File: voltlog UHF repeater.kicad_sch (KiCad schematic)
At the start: 40 parts, among them J1 Conn_02x13_Odd_Even, J2 Conn_01x13, J3 Conn_Coaxial, Q1 BC847, Q2 BC857, U1 SA818

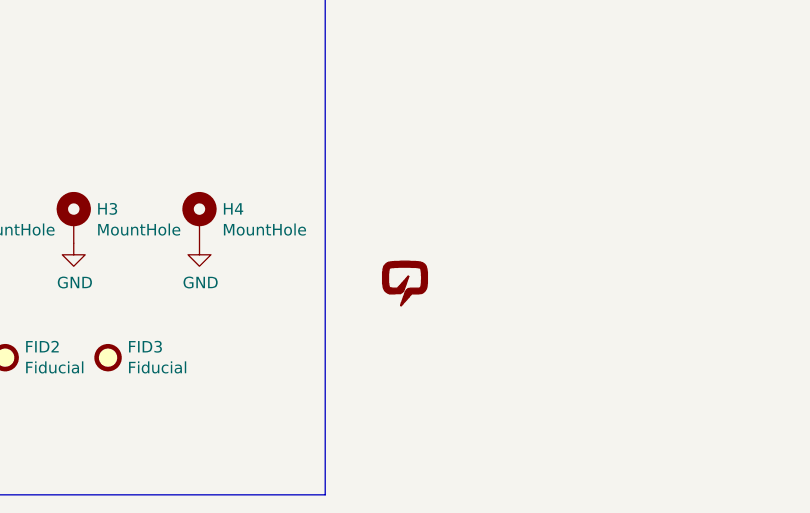
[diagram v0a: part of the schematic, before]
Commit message: Removed logo from schemantic. Removed H1-H4, Fid1-Fid3, J1, J2 and JP1 from BOM and POS file.
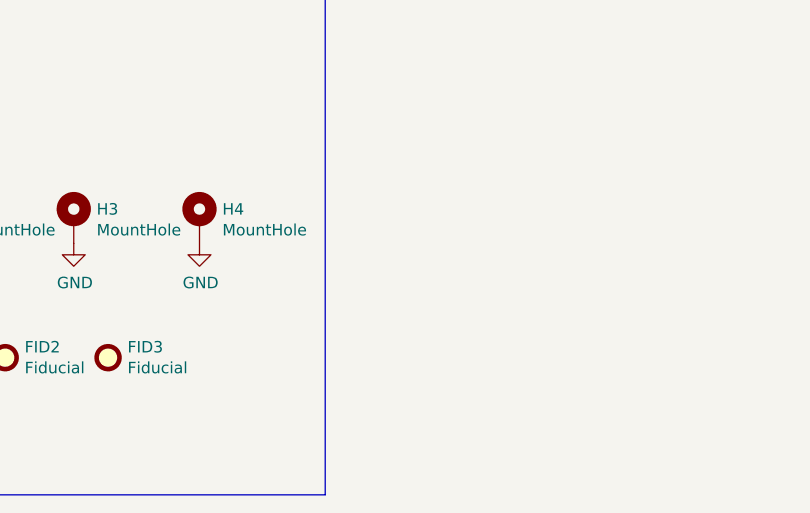
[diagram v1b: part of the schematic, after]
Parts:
- removed V1: VOLTLOG_LOGO, Voltlog:voltlog_mask_3mm, symbol voltlog UHF repeater-rescue:VOLTLOG_LOGO-voltlog
- H1, H2, H3, H4: now left out of the parts list
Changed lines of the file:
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@@
   )
   (symbol (lib_id "Connector_Generic:Conn_02x13_Odd_Even") (at 44.45 168.91 0) (unit 1)
-    (in_bom yes) (on_board yes) (dnp no)
+    (in_bom yes) (on_board no) (dnp no)
     (property "Reference" "J1" (at 45.72 148.1582 0)
       (effects (font (size 1.27 1.27)))
@@
   )
   (symbol (lib_id "Connector_Generic:Conn_01x13") (at 90.17 168.91 0) (unit 1)
-    (in_bom yes) (on_board yes) (dnp no)
+    (in_bom yes) (on_board no) (dnp no)
     (property "Reference" "J2" (at 92.202 167.8432 0)
       (effects (font (size 1.27 1.27)) (justify left))
@@
   )
   (symbol (lib_id "Mechanical:Fiducial") (at 127 179.07 0) (unit 1)
-    (in_bom no) (on_board yes) (dnp no)
+    (in_bom no) (on_board no) (dnp no)
     (property "Reference" "FID1" (at 129.159 177.9016 0)
       (effects (font (size 1.27 1.27)) (justify left))
@@
   )
   (symbol (lib_id "Mechanical:Fiducial") (at 138.43 179.07 0) (unit 1)
-    (in_bom no) (on_board yes) (dnp no)
+    (in_bom no) (on_board no) (dnp no)
     (property "Reference" "FID2" (at 140.589 177.9016 0)
       (effects (font (size 1.27 1.27)) (justify left))
@@
   )
   (symbol (lib_id "Mechanical:Fiducial") (at 149.86 179.07 0) (unit 1)
-    (in_bom no) (on_board yes) (dnp no)
+    (in_bom no) (on_board no) (dnp no)
     (property "Reference" "FID3" (at 152.019 177.9016 0)
       (effects (font (size 1.27 1.27)) (justify left))
@@
   )
   (symbol (lib_id "Mechanical:MountingHole_Pad") (at 118.11 163.83 0) (unit 1)
-    (in_bom yes) (on_board yes) (dnp no)
+    (in_bom no) (on_board no) (dnp no)
     (property "Reference" "H1" (at 120.65 162.5854 0)
       (effects (font (size 1.27 1.27)) (justify left))
@@
   )
   (symbol (lib_id "Mechanical:MountingHole_Pad") (at 132.08 163.83 0) (unit 1)
-    (in_bom yes) (on_board yes) (dnp no)
+    (in_bom no) (on_board no) (dnp no)
     (property "Reference" "H2" (at 134.62 162.5854 0)
       (effects (font (size 1.27 1.27)) (justify left))
@@
   )
   (symbol (lib_id "Mechanical:MountingHole_Pad") (at 146.05 163.83 0) (unit 1)
-    (in_bom yes) (on_board yes) (dnp no)
+    (in_bom no) (on_board no) (dnp no)
     (property "Reference" "H3" (at 148.59 162.5854 0)
       (effects (font (size 1.27 1.27)) (justify left))
@@
   )
   (symbol (lib_id "Mechanical:MountingHole_Pad") (at 160.02 163.83 0) (unit 1)
-    (in_bom yes) (on_board yes) (dnp no)
+    (in_bom no) (on_board no) (dnp no)
     (property "Reference" "H4" (at 162.56 162.5854 0)
       (effects (font (size 1.27 1.27)) (justify left))
@@
         )
       )
-    )
-  )
-  (symbol (lib_id "voltlog UHF repeater-rescue:VOLTLOG_LOGO-voltlog") (at 182.88 170.18 0) (unit 1)
-    (in_bom yes) (on_board yes) (dnp no)
-    (property "Reference" "V1" (at 182.88 173.482 0)
-      (effects (font (size 1.524 1.524)) hide)
-    )
-    (property "Value" "VOLTLOG_LOGO" (at 182.88 166.878 0)
-      (effects (font (size 1.524 1.524)) hide)
-    )
-    (property "Footprint" "Voltlog:voltlog_mask_3mm" (at 182.88 170.18 0)
-      (effects (font (size 1.27 1.27)) hide)
-    )
-    (property "Datasheet" "" (at 182.88 170.18 0)
-      (effects (font (size 1.27 1.27)) hide)
-    )
-    (instances
-      (project "voltlog UHF repeater"
-        (path "/96804582-7319-485a-be7b-2a888b98bdd6"
-          (reference "V1") (unit 1)
-        )
-      )
